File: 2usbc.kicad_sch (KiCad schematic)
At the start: 20 parts, among them J101 USB_C_Plug_USB2.0, J102 USB_C_Receptacle_USB2.0, J103 USB_C_Receptacle_USB2.0, U101 TLV76733DRVx, U102 USBLC6-2SC6

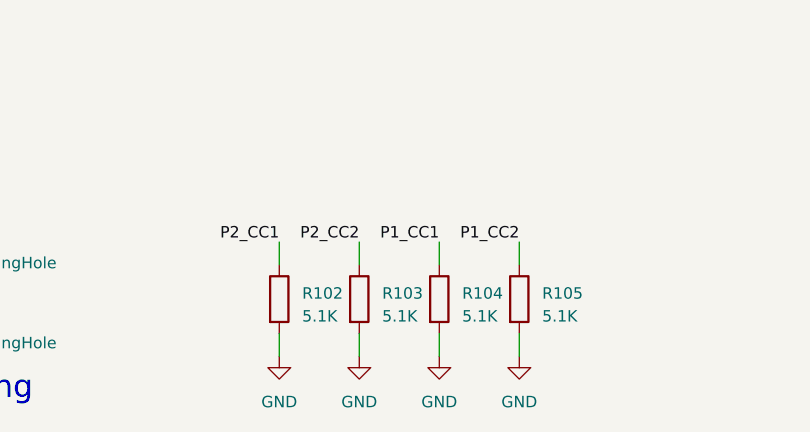
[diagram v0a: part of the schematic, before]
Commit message: Update CC resistors with feedback
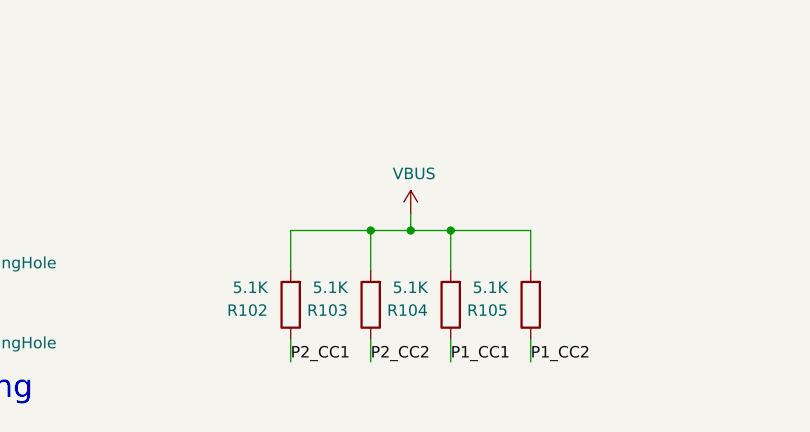
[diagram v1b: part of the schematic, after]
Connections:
- net GND: no longer R102.2, R103.2, R104.2, R105.2
- net VBUS: now also R102.2, R103.2, R104.2, R105.2
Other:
- moved on the sheet: R102, R103, R104, R105

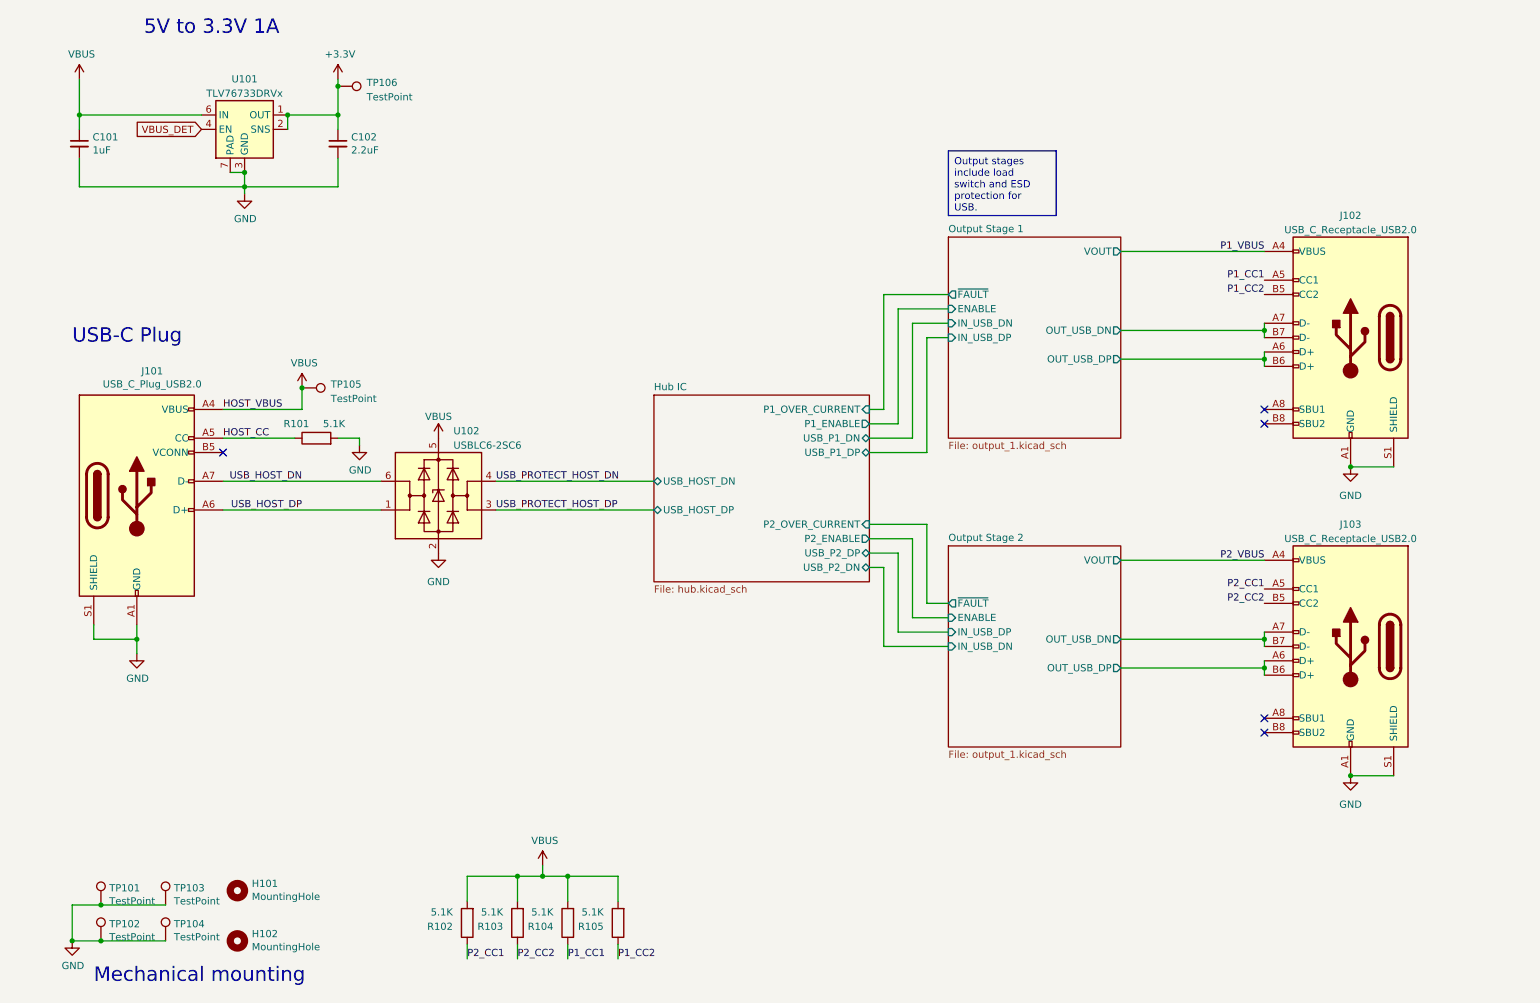
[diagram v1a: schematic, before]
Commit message: Add power switch ic and channel config ic
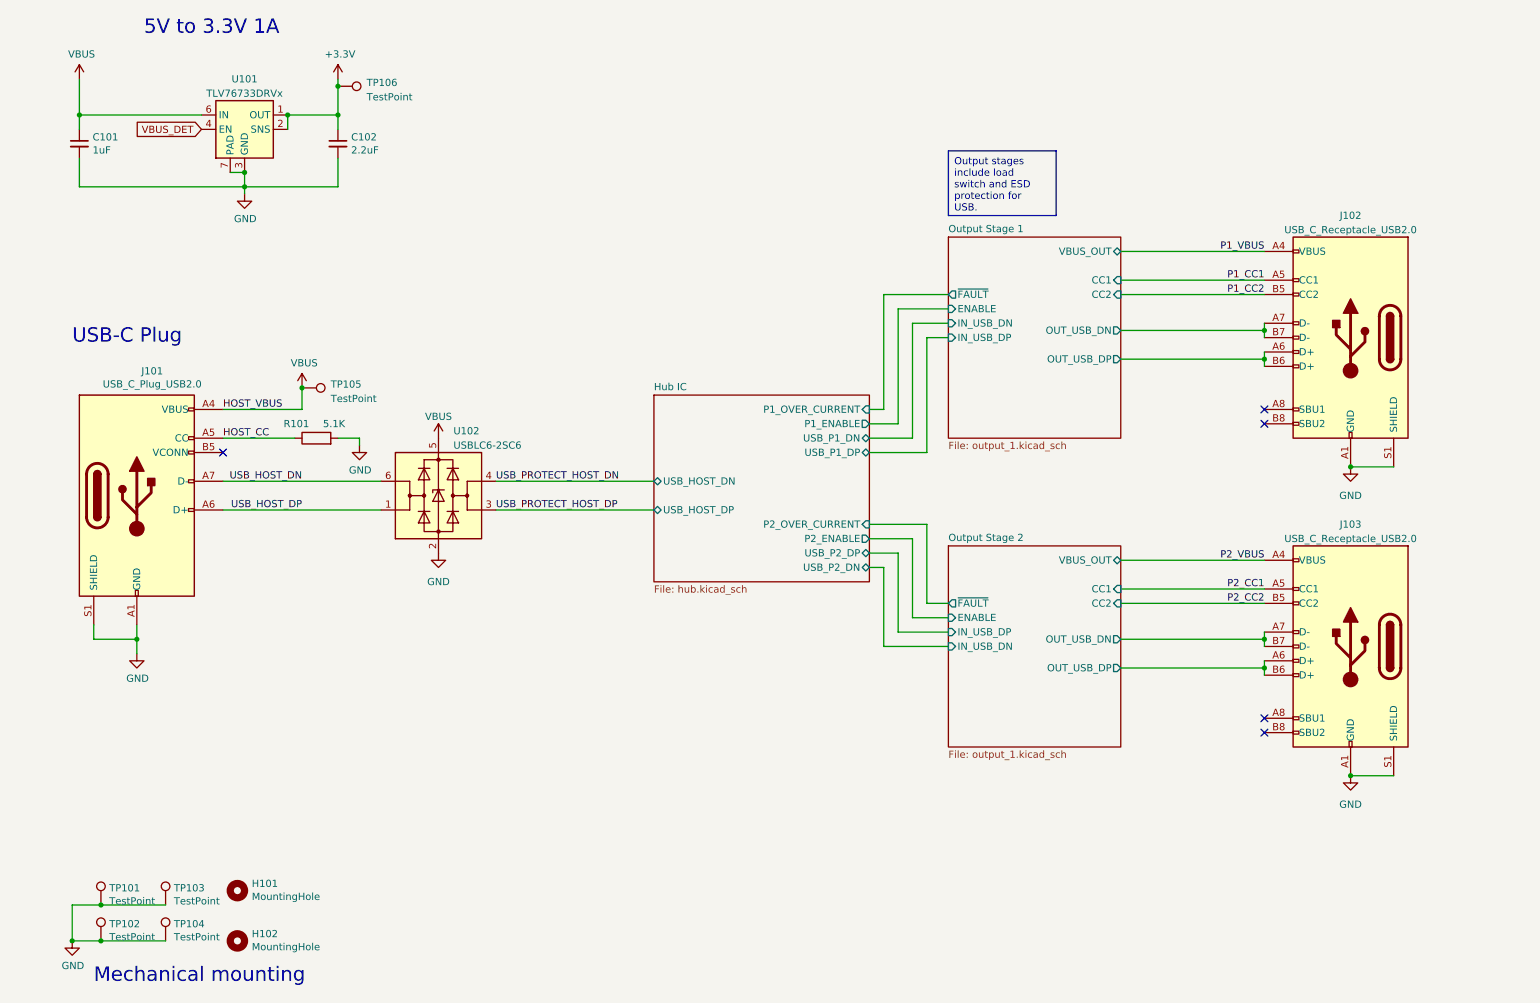
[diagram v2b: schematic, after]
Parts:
- removed R102, R103, R104, R105: 5.1K, Resistor_SMD:R_0201_0603Metric, symbol Device:R
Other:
- sheet Output Stage 1 ports: added CC1, CC2, VBUS_OUT; removed VOUT
- sheet Output Stage 2 ports: added CC1, CC2, VBUS_OUT; removed VOUT

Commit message: Layout checkpoint
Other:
- note added: "DFP"
- note added: "UFP"
- moved on the sheet: H101, H102, TP101, TP102, TP103, TP104

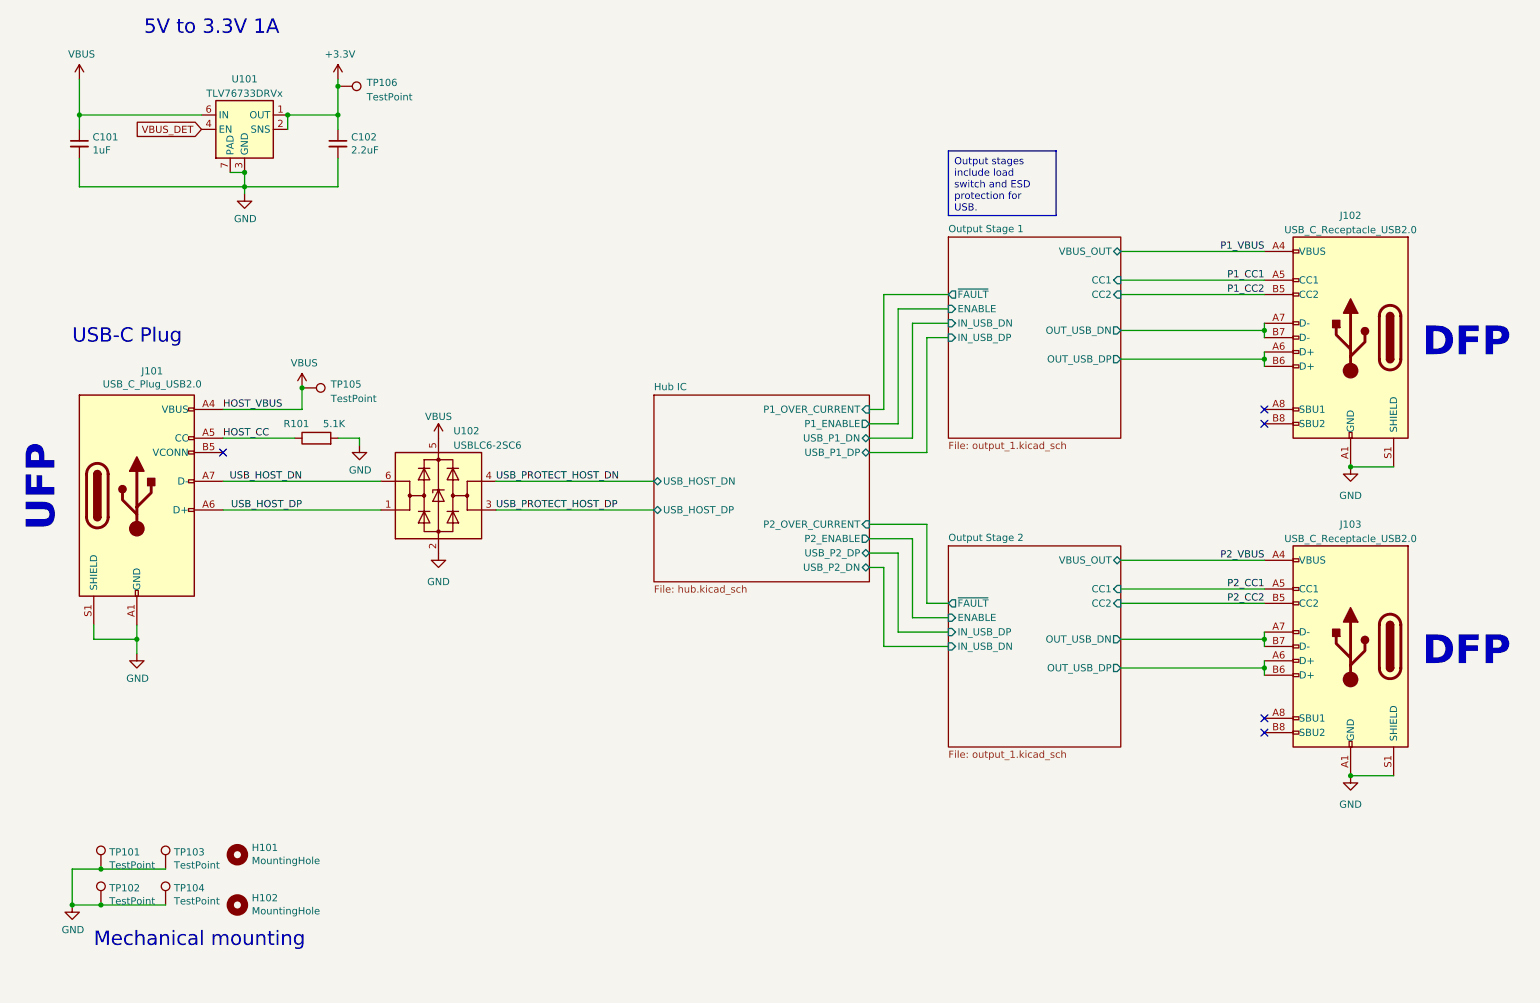
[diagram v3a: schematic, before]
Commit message: Update schematic with feedback
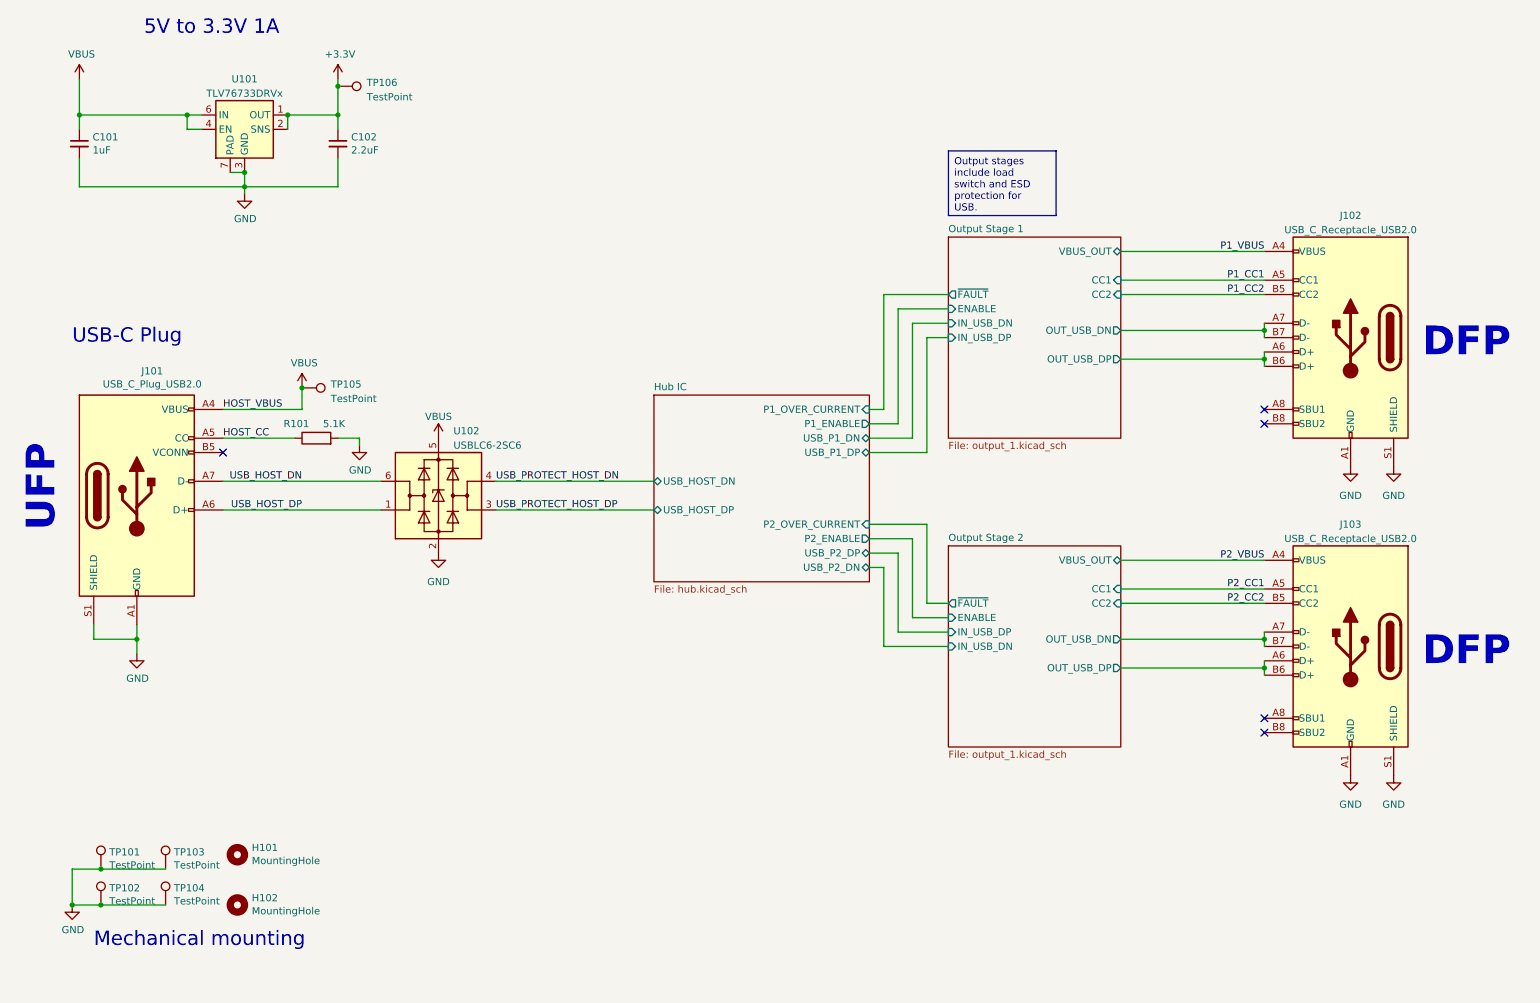
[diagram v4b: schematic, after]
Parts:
- J101: MPN (none) -> 105444; Manufacturer (none) -> Molex
- J102, J103: footprint 2usb:MOLEX_2169900003 -> 2usb:USB4520; MPN (none) -> USB4520-03-0-A; Manufacturer (none) -> Global Connector Technology
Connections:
- net VBUS_DET is gone; now on net VBUS: U101.4 (EN)
